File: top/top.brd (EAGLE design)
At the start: 38 x 22 mm, 10 parts, among them X1 52745-1290

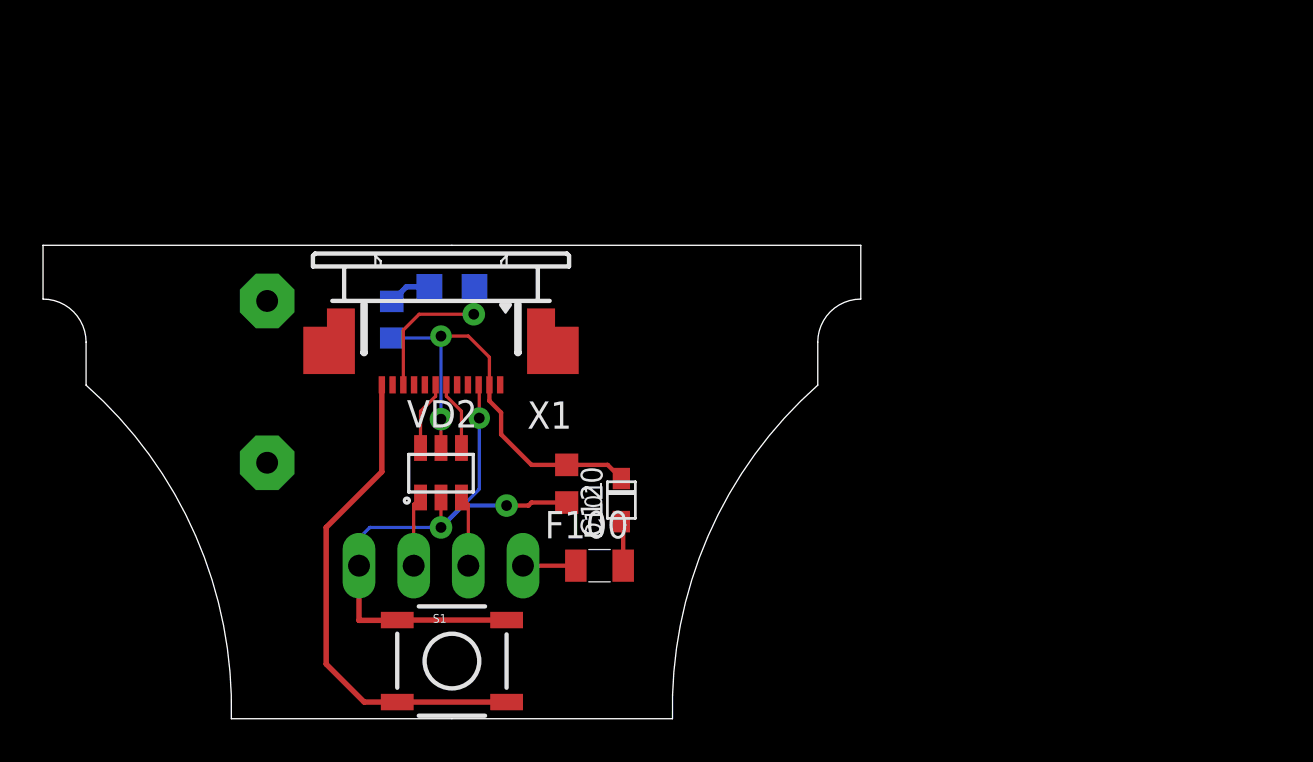
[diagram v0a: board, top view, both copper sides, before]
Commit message: Added silkscreen texts
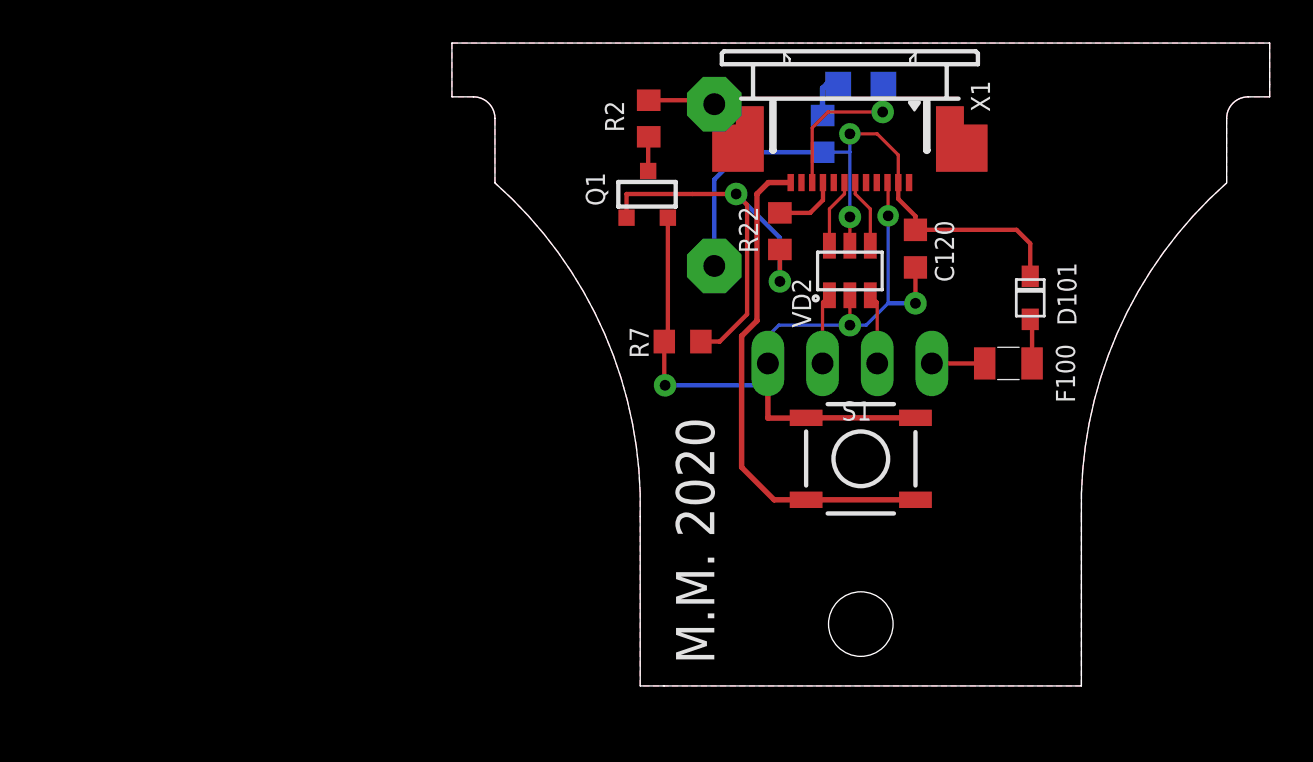
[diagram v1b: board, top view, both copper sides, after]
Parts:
- added Q1: TSM2302CX, transistors:SOT-23
- added R2, R22: 10, rcl:R0603
- added R7: 10k, rcl:R0603
- moved SP1 22.7 mm to (12.2, 24.8)
- moved R1 21.8 mm to (17.2, 27.2)
- moved D101 21.2 mm to (26.9, 19.6)
- moved F100 21.2 mm to (25.9, 16.5)
- moved JP1 21.2 mm to (18.5, 16.5)
- moved LED2 21.2 mm to (19.0, 29.5)
- moved S1 21.2 mm to (19.0, 12.1)
- moved VD2 21.2 mm to (18.5, 20.8)
- moved X1 21.2 mm to (18.5, 27.4)
- moved C120 19.5 mm to (21.5, 21.8)
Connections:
- net N$1 renamed LED_R
- removed net BPR: X1.9
- removed net BUZZER_PLUS: SP1.1
- new net BEEPER: R22.1, X1.9
- new net BEEPER_FET_DRAIN: Q1.3, R2.1
- new net BEEPER_R: R2.2, SP1.2
- new net BUZZER_BEFORERES: Q1.1, R22.2, R7.1
- net GND: now also Q1.2, R7.2
- net VUSB: now also SP1.1
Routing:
- net BUZZER_BEFORERES: track 0.00 -> 21.1 mm, vias 0 -> 2
- net GND: track 29.8 -> 40.3 mm, vias 3 -> 4
- net VUSB: track 20.4 -> 29.6 mm
- net BEEPER_R: track 0.00 -> 3.12 mm
- net BEEPER: track 0.00 -> 3.06 mm
- net BEEPER_FET_DRAIN: track 0.00 -> 1.60 mm
- added copper zone on layer 1, net GND
- added copper zone on layer 16, net GND
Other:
- board size 38 x 22 mm -> 38 x 29.9 mm
- board text added: "GND BK D+ GN D- WH VUSB RD"
- board text added: "M.M. 2020"
